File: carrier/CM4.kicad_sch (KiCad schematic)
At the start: 29 parts, among them J2 52271-0879, J3 Micro_SD_Card, J7 AudioJack3_Switch, U4 AP22814AW5

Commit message: pcb
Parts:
- removed TP27: AUXR, TestPoint:TestPoint_Pad_1.0x1.0mm, symbol Connector:TestPoint
- removed TP28: AUXL, TestPoint:TestPoint_Pad_1.0x1.0mm, symbol Connector:TestPoint
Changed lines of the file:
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@@
   (junction (at 174.625 160.02) (diameter 0.9144) (color 0 0 0 0))
   (junction (at 189.23 122.555) (diameter 0.9144) (color 0 0 0 0))
-  (junction (at 191.77 122.555) (diameter 0.9144) (color 0 0 0 0))
-  (junction (at 205.74 129.54) (diameter 0.9144) (color 0 0 0 0))
   (junction (at 210.82 80.01) (diameter 0.9144) (color 0 0 0 0))
   (junction (at 246.38 24.765) (diameter 0.9144) (color 0 0 0 0))
@@
     (stroke (width 0) (type solid) (color 0 0 0 0))
   )
-  (wire (pts (xy 191.77 120.015) (xy 191.77 122.555))
-    (stroke (width 0) (type solid) (color 0 0 0 0))
-  )
-  (wire (pts (xy 191.77 122.555) (xy 189.23 122.555))
+  (wire (pts (xy 189.23 122.555) (xy 201.295 122.555))
     (stroke (width 0) (type solid) (color 0 0 0 0))
   )
@@
     (stroke (width 0) (type solid) (color 0 0 0 0))
   )
+  (wire (pts (xy 196.215 129.54) (xy 207.645 129.54))
+    (stroke (width 0) (type solid) (color 0 0 0 0))
+  )
   (wire (pts (xy 196.215 139.065) (xy 171.45 139.065))
     (stroke (width 0) (type solid) (color 0 0 0 0))
   )
-  (wire (pts (xy 201.295 122.555) (xy 191.77 122.555))
-    (stroke (width 0) (type solid) (color 0 0 0 0))
-  )
   (wire (pts (xy 201.295 134.62) (xy 201.295 122.555))
     (stroke (width 0) (type solid) (color 0 0 0 0))
@@
   )
   (wire (pts (xy 201.93 141.605) (xy 201.93 139.7))
-    (stroke (width 0) (type solid) (color 0 0 0 0))
-  )
-  (wire (pts (xy 205.74 123.825) (xy 205.74 129.54))
-    (stroke (width 0) (type solid) (color 0 0 0 0))
-  )
-  (wire (pts (xy 205.74 129.54) (xy 196.215 129.54))
-    (stroke (width 0) (type solid) (color 0 0 0 0))
-  )
-  (wire (pts (xy 207.645 129.54) (xy 205.74 129.54))
     (stroke (width 0) (type solid) (color 0 0 0 0))
   )
@@
       (effects (font (size 1.27 1.27)) hide)
     )
-    (pin "1")
-  )
-  (symbol (lib_id "Connector:TestPoint") (at 191.77 120.015 0) (unit 1)
-    (in_bom yes) (on_board yes) (fields_autoplaced)
-    (property "Reference" "TP27" (id 0) (at 194.31 116.9034 0)
-      (effects (font (size 1.27 1.27)) (justify left))
-    )
-    (property "Value" "AUXR" (id 1) (at 194.31 119.4434 0)
-      (effects (font (size 1.27 1.27)) (justify left))
-    )
-    (property "Footprint" "TestPoint:TestPoint_Pad_1.0x1.0mm" (id 2) (at 196.85 120.015 0)
-      (effects (font (size 1.27 1.27)) hide)
-    )
-    (property "Datasheet" "~" (id 3) (at 196.85 120.015 0)
-      (effects (font (size 1.27 1.27)) hide)
-    )
-    (pin "1")
-  )
-  (symbol (lib_id "Connector:TestPoint") (at 205.74 123.825 0) (unit 1)
-    (in_bom yes) (on_board yes) (fields_autoplaced)
-    (property "Reference" "TP28" (id 0) (at 207.645 120.7134 0)
-      (effects (font (size 1.27 1.27)) (justify left))
-    )
-    (property "Value" "AUXL" (id 1) (at 207.645 123.2534 0)
-      (effects (font (size 1.27 1.27)) (justify left))
-    )
-    (property "Footprint" "TestPoint:TestPoint_Pad_1.0x1.0mm" (id 2) (at 210.82 123.825 0)
-      (effects (font (size 1.27 1.27)) hide)
-    )
-    (property "Datasheet" "~" (id 3) (at 210.82 123.825 0)
-      (effects (font (size 1.27 1.27)) hide)
-    )

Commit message: aaaa
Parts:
- removed TP2: Activity, TestPoint:TestPoint_Pad_1.0x1.0mm, symbol Connector:TestPoint
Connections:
- net BTN_SELECT: now also Module0.55 (GPIO14); no longer Module0.25 (GPIO21)
- net BTN_START: now also Module0.25 (GPIO21); no longer Module0.45 (GPIO24)
- net DPAD_DOWN: no longer Module0.55 (GPIO14)
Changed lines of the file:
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@@
   (junction (at 101.6 109.22) (diameter 0.9144) (color 0 0 0 0))
   (junction (at 101.6 116.84) (diameter 0.9144) (color 0 0 0 0))
-  (junction (at 112.395 43.18) (diameter 0.9144) (color 0 0 0 0))
   (junction (at 136.525 139.065) (diameter 0.9144) (color 0 0 0 0))
   (junction (at 136.525 140.97) (diameter 0.9144) (color 0 0 0 0))
@@
     (stroke (width 0) (type solid) (color 0 0 0 0))
   )
-  (wire (pts (xy 112.395 40.64) (xy 112.395 43.18))
-    (stroke (width 0) (type solid) (color 0 0 0 0))
-  )
-  (wire (pts (xy 112.395 43.18) (xy 112.395 44.45))
-    (stroke (width 0) (type solid) (color 0 0 0 0))
-  )
-  (wire (pts (xy 112.395 43.18) (xy 118.11 43.18))
+  (wire (pts (xy 112.395 40.64) (xy 112.395 44.45))
     (stroke (width 0) (type solid) (color 0 0 0 0))
   )
@@
     (effects (font (size 1.27 1.27)) (justify right))
   )
-  (hierarchical_label "BTN_SELECT" (shape input) (at 103.505 58.42 0)
+  (hierarchical_label "BTN_START" (shape input) (at 103.505 58.42 0)
     (effects (font (size 1.27 1.27)) (justify left))
   )
@@
     (effects (font (size 1.27 1.27)) (justify left))
   )
-  (hierarchical_label "BTN_START" (shape input) (at 103.505 83.82 0)
-    (effects (font (size 1.27 1.27)) (justify left))
-  )
   (hierarchical_label "SHOULDER_R" (shape input) (at 103.505 86.36 0)
     (effects (font (size 1.27 1.27)) (justify left))
   )
-  (hierarchical_label "DPAD_DOWN" (shape input) (at 103.505 96.52 0)
+  (hierarchical_label "BTN_SELECT" (shape input) (at 103.505 96.52 0)
     (effects (font (size 1.27 1.27)) (justify left))
   )
@@
     (effects (font (size 1.27 1.27)) (justify left))
   )
-  (symbol (lib_id "Connector:TestPoint") (at 118.11 43.18 270) (unit 1)
-    (in_bom yes) (on_board yes) (fields_autoplaced)
-    (property "Reference" "TP2" (id 0) (at 123.19 41.9099 90)
-      (effects (font (size 1.27 1.27)) (justify left))
-    )
-    (property "Value" "Activity" (id 1) (at 123.19 44.4499 90)
-      (effects (font (size 1.27 1.27)) (justify left))
-    )
-    (property "Footprint" "TestPoint:TestPoint_Pad_1.0x1.0mm" (id 2) (at 118.11 48.26 0)
-      (effects (font (size 1.27 1.27)) hide)
-    )
-    (property "Datasheet" "~" (id 3) (at 118.11 48.26 0)
-      (effects (font (size 1.27 1.27)) hide)
-    )
-    (pin "1")
+  (hierarchical_label "DPAD_DOWN" (shape input) (at 118.11 96.52 0)
+    (effects (font (size 1.27 1.27)) (justify left))
   )
   (symbol (lib_id "Connector:TestPoint") (at 272.415 27.94 270) (unit 1)

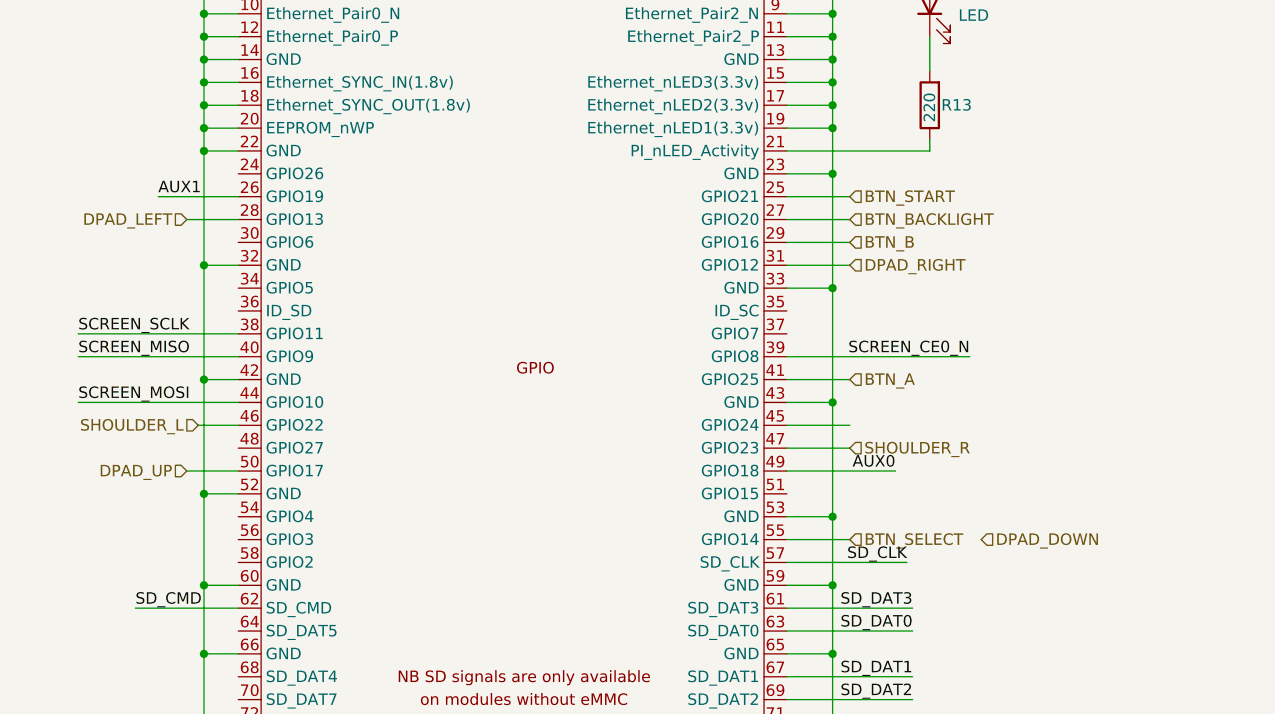
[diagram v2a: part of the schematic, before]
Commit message: getting back into the swing of this
aded some stuff for the resistors, moved some stuff about, removed the schmitt inverter (software is the solution for all our problems, forever)
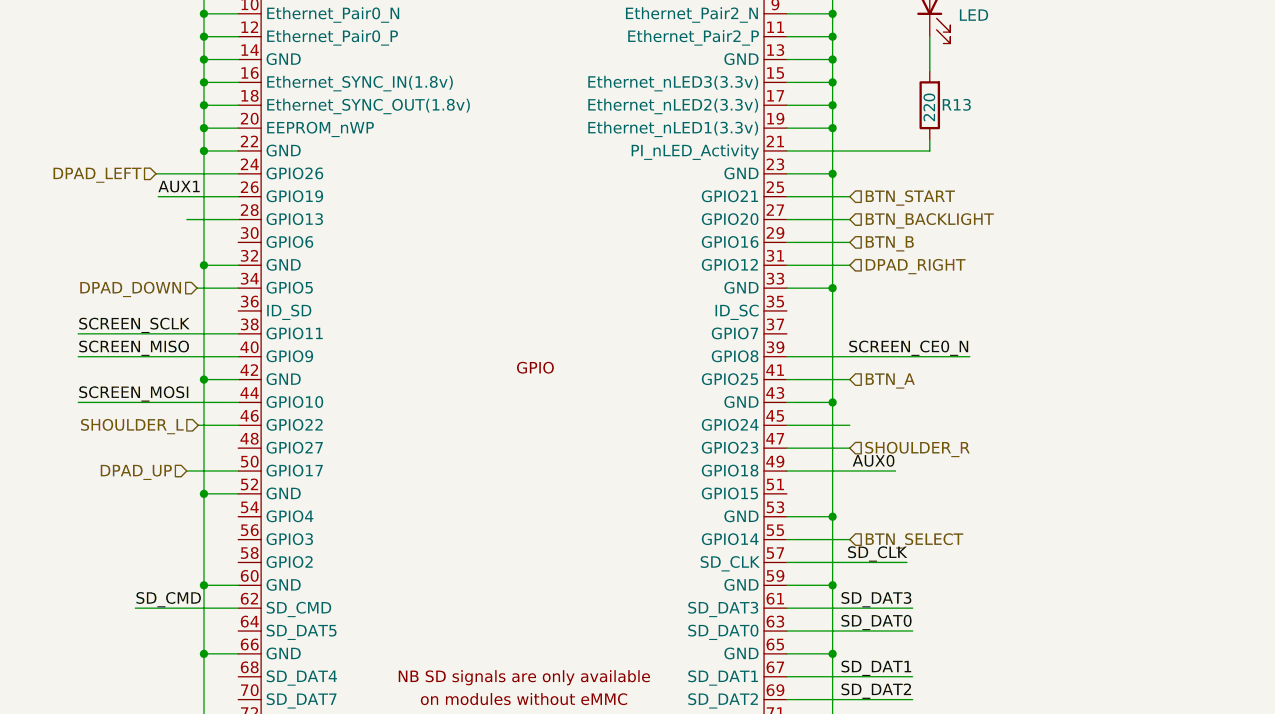
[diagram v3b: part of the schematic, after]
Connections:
- net DPAD_DOWN: now also Module0.34 (GPIO5)
- net DPAD_LEFT: now also Module0.24 (GPIO26); no longer Module0.28 (GPIO13)
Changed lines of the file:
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@@
     (stroke (width 0) (type solid) (color 0 0 0 0))
+  )
+  (wire (pts (xy 26.416 55.88) (xy 35.56 55.88))
+    (stroke (width 0) (type default) (color 0 0 0 0))
   )
   (wire (pts (xy 26.67 58.42) (xy 35.56 58.42))
@@
   (wire (pts (xy 29.845 88.9) (xy 35.56 88.9))
     (stroke (width 0) (type solid) (color 0 0 0 0))
+  )
+  (wire (pts (xy 30.988 68.58) (xy 35.56 68.58))
+    (stroke (width 0) (type default) (color 0 0 0 0))
   )
   (wire (pts (xy 31.115 83.82) (xy 35.56 83.82))
@@
     (effects (font (size 1.27 1.27)) (justify right))
   )
+  (hierarchical_label "DPAD_LEFT" (shape input) (at 26.416 55.88 180)
+    (effects (font (size 1.27 1.27)) (justify right))
+  )
   (hierarchical_label "FUEL_SCL" (shape output) (at 27.94 127 180)
     (effects (font (size 1.27 1.27)) (justify right))
@@
     (effects (font (size 1.27 1.27)) (justify right))
   )
-  (hierarchical_label "DPAD_LEFT" (shape input) (at 29.845 60.96 180)
-    (effects (font (size 1.27 1.27)) (justify right))
-  )
   (hierarchical_label "DPAD_UP" (shape input) (at 29.845 88.9 180)
     (effects (font (size 1.27 1.27)) (justify right))
   )
+  (hierarchical_label "DPAD_DOWN" (shape input) (at 30.988 68.58 180)
+    (effects (font (size 1.27 1.27)) (justify right))
+  )
   (hierarchical_label "SHOULDER_L" (shape input) (at 31.115 83.82 180)
     (effects (font (size 1.27 1.27)) (justify right))
@@
     (effects (font (size 1.27 1.27)) (justify left))
   )
-  (hierarchical_label "DPAD_DOWN" (shape input) (at 118.11 96.52 0)
-    (effects (font (size 1.27 1.27)) (justify left))
-  )

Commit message: aa
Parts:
- added LS?: Speaker, symbol Device:Speaker
- added Q?: 2N2219, Package_TO_SOT_THT:TO-39-3, symbol Transistor_BJT:2N2219
- added R?: 1M, symbol Device:R
- added R?: 15k, symbol Device:R
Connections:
- net +3.3v: now also R?.1
- net AUX0: now also R14.1; no longer R23.1
- net AUX1: now also R23.1; no longer R14.1
- net GND: now also R18.1, Q?.1 (E); no longer R18.2
- net at C7.2, C9.1, R14.2: now also R18.2; no longer R18.1
- net at J7.RN: now also Q?.2 (B), R?.2
- net AUX_DETECT: now reaches J7.SN
- net AUX_DETECT: now also R?.2
- new net: LS?.2, Q?.3 (C)
- new net: LS?.1, R?.1
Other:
- note added: "GRID IS 25 MIL EVERYWEHRE"
- note added: "gbasp speaker is 8ohm"
- note added: "hot tip: simple speaker detect *should* work here connect RN as aux detect, but when there is no signal we can push to speaker."
- note added: "should probably test this on a board first!"
- note added: "weak pull up when a jack is connected (SN is disconnected) - AUX_DETECT is 1 when no jack, there is a pulldown to ground that will be preferred - AUX_DETECT is 0"
- note removed: "close relative part to whats on the cm4io's sheet"
- moved on the sheet: C23, C24, C7, C9, D4, D5, J7, R14, R18, R23, R24

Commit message: thingy
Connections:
- net +5v: now also LS?.1, R?.1
- net BTN_SELECT: now also Module0.51 (GPIO15); no longer Module0.55 (GPIO14)
- new net TXD_POW: Module0.55 (GPIO14)
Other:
- note added: "UART needs enable - TXD is data transmit Is default pull up - can be used as a power switch on OS shutdown OS Shutdown --> Trip Power"

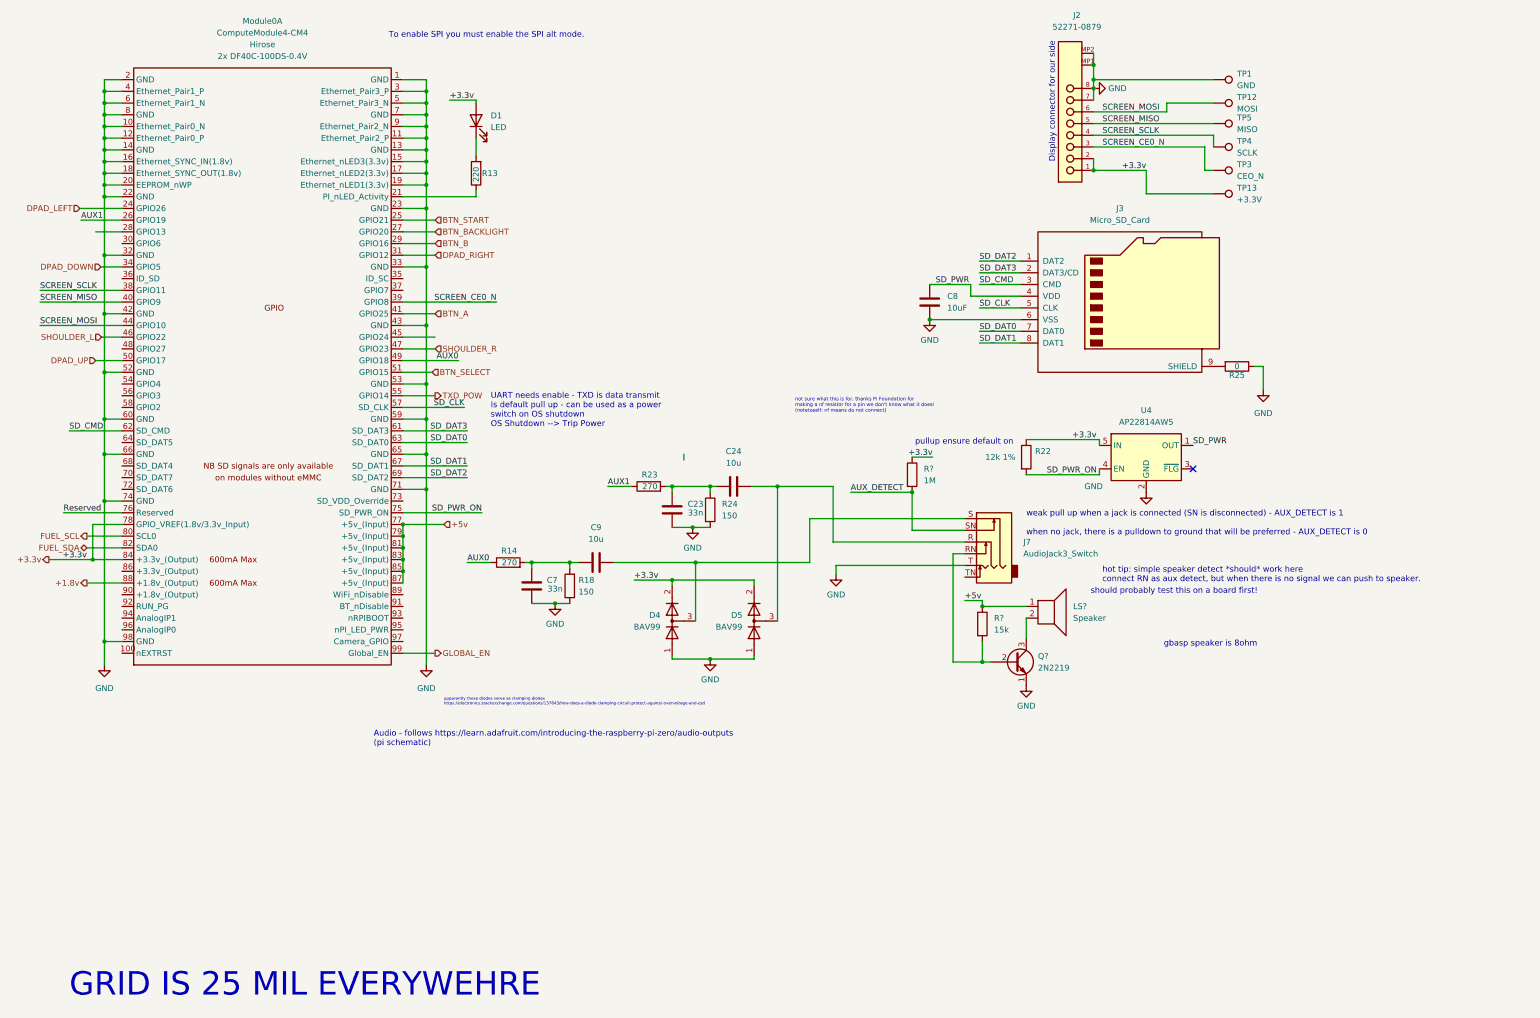
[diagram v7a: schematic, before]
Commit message: fixed switching and added fuel gague
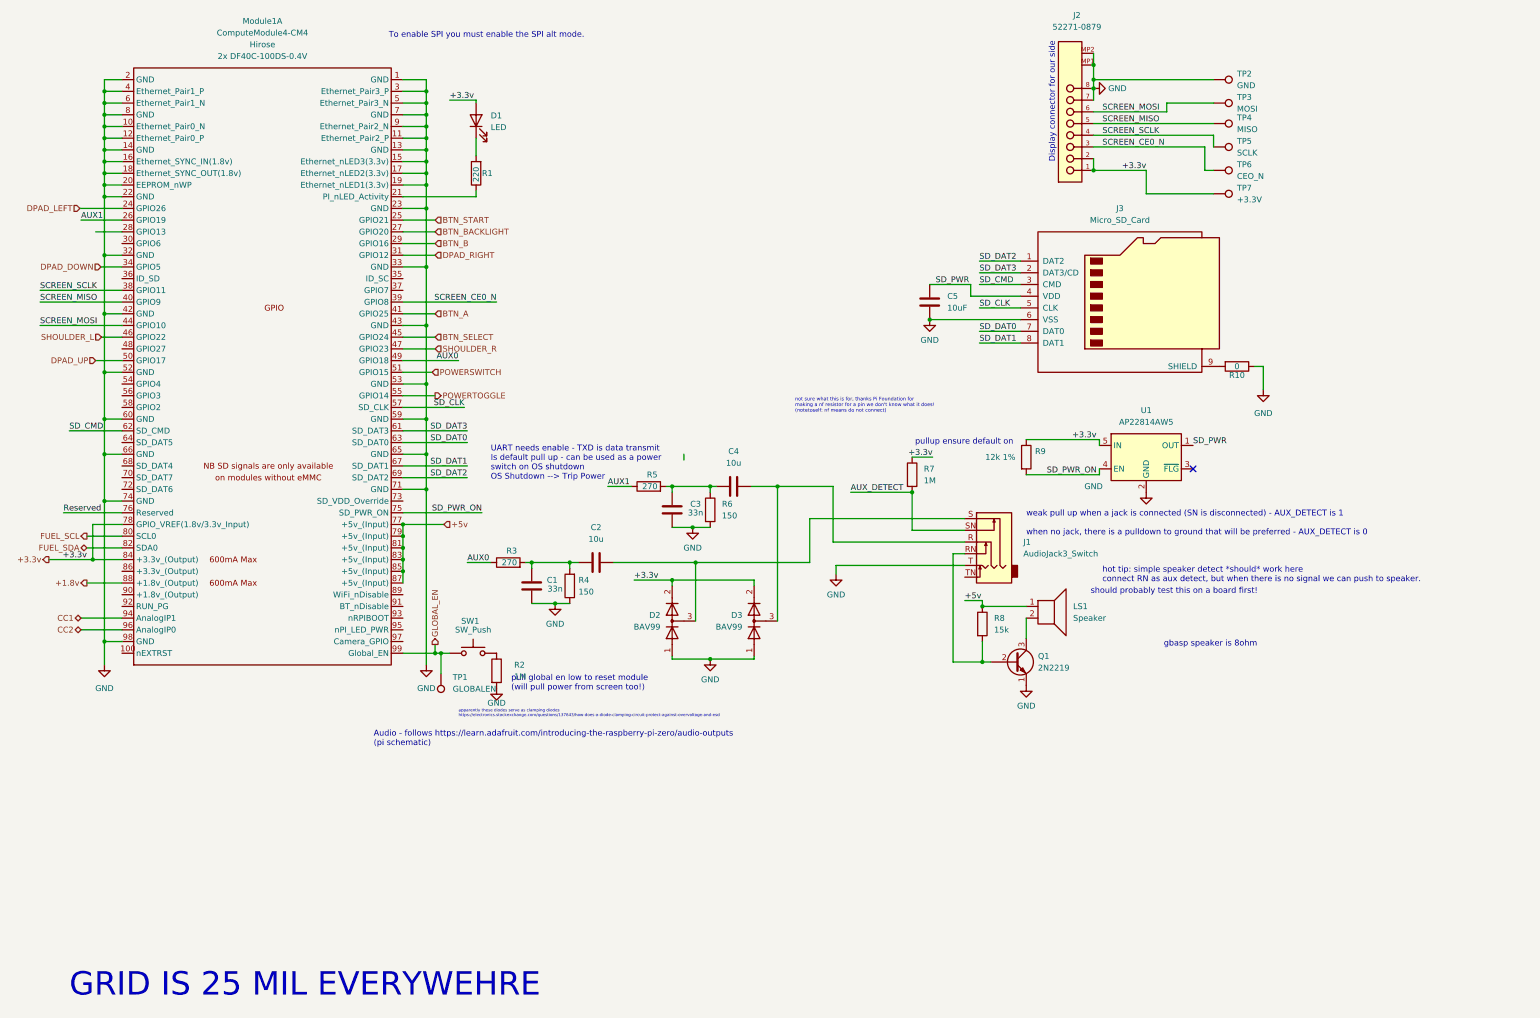
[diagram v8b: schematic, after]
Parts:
- added R2: 1M, symbol Device:R
- added SW1: SW_Push, symbol Switch:SW_Push
- added TP1: GLOBALEN, symbol Connector:TestPoint
- gave numbers to parts that had none: 4
- renumbered C7 to C1, C9 to C2, C23 to C3, C24 to C4, C8 to C5, D4 to D2, D5 to D3, J7 to J1, Module0 to Module1, R13 to R1, R25 to R10, R14 to R3, R18 to R4, R23 to R5, R24 to R6, R22 to R9, TP1 to TP2, TP12 to TP3, TP5 to TP4, TP4 to TP5, TP3 to TP6, TP13 to TP7, U4 to U1
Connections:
- net BTN_SELECT: now also Module1.45 (GPIO24); no longer Module1.51 (GPIO15)
- net GLOBAL_EN: now also SW1.1, TP1.1
- net GND: now also R2.2
- net CC1: now reaches Module1.94 (AnalogIP1)
- net CC2: now reaches Module1.96 (AnalogIP0)
- net TXD_POW renamed POWERTOGGLE
- new net: R2.1, SW1.2
- new net POWERSWITCH: Module1.51 (GPIO15)
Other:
- note added: "pull global en low to reset module (will pull power from screen too!)"
